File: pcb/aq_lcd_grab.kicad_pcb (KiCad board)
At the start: 4 copper layers, 32 x 50 mm, 29 parts, among them J1 Conn_01x39_Socket, J2 Conn_01x39_Socket, J3 Conn_01x03_Socket, J4 Conn_01x02_Socket, J5 Conn_01x03_Pin, U1 STM32F103C8Tx, U2 Conn_01x14

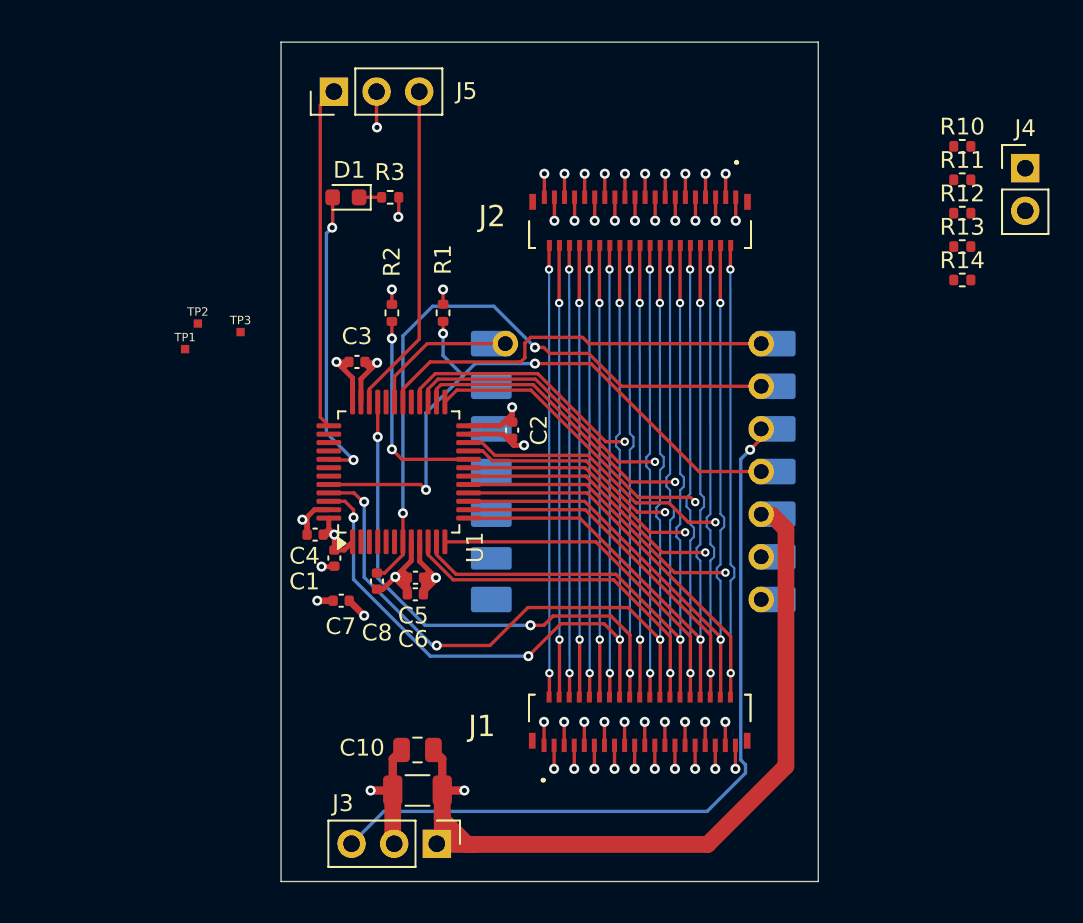
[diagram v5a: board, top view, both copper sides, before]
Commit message: PCB: routing pass — more traces, placement nudges, zone refill
Manual layout work on the KiCad PCB: ~32 net-new trace segments,
a couple of additional vias, and ~80 placement adjustments. Zone
fills recomputed against the new geometry. No SKiDL/netlist
changes — this is layout work on top of the existing netlist.

Co-Authored-By: Claude Opus 4.7 (1M context) <noreply@anthropic.com>
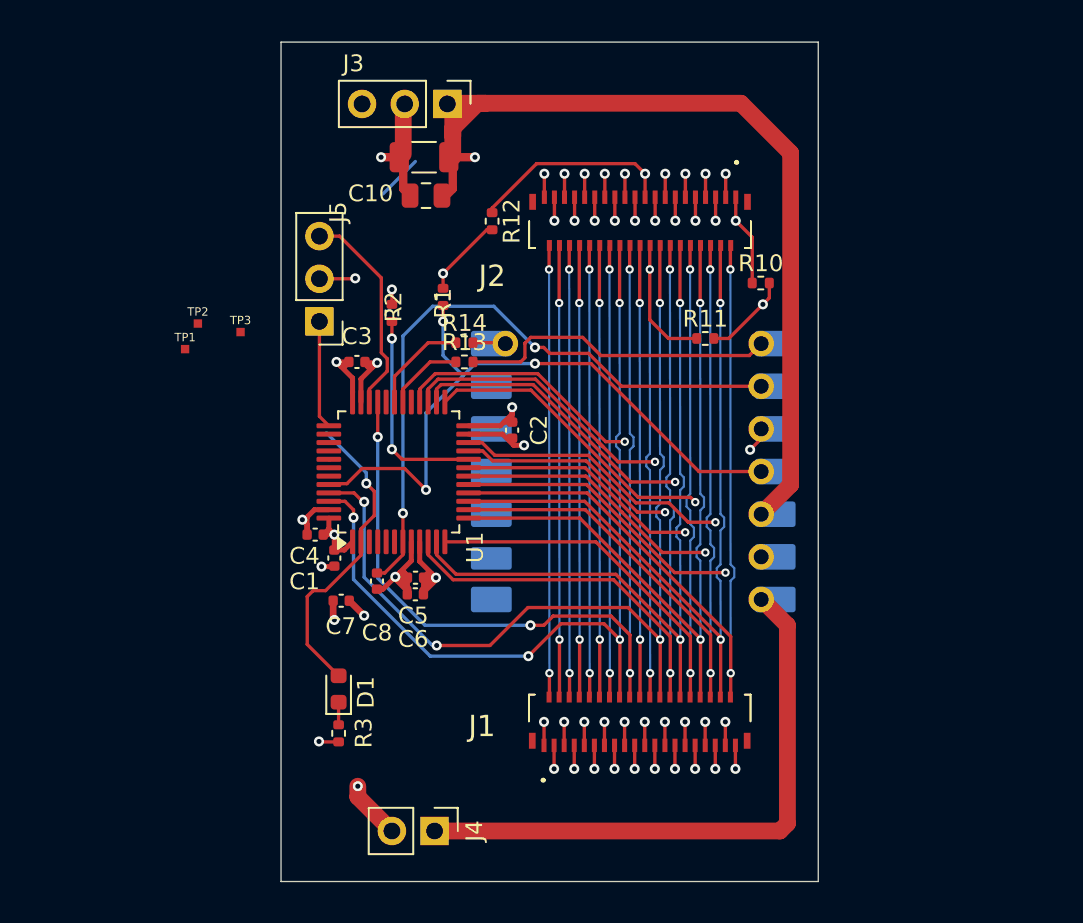
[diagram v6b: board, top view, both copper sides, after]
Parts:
- moved J4 52.9 mm to (59.9, 72.4), turned to -90 degrees
- moved J3 44.1 mm to (60.7, 29.1)
- moved C11 37.7 mm to (59.3, 32.3)
- moved C10 33.0 mm to (59.4, 34.5)
- moved R3 32.1 mm to (54.2, 66.6), turned to 90 degrees
- moved R13 30.4 mm to (61.7, 44.5)
- moved R14 29.9 mm to (61.7, 43.3)
- moved D1 29.3 mm to (54.2, 63.9), turned to 90 degrees
- moved R12 28.0 mm to (63.4, 36.1), turned to -90 degrees
- moved R11 18.0 mm to (76.1, 43.1)
- moved R10 14.5 mm to (79.4, 39.8)
- moved J5 13.7 mm to (53.1, 42.0), turned to 180 degrees
- moved R1 0.95 mm to (60.5, 40.6)
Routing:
- net PIC32_RESET: track 46.3 -> 4.24 mm
- net +5V: track 0.00 -> 35.2 mm
- net UART_STM_TX: track 24.0 -> 4.59 mm
- net UART_ESP_RX: track 0.00 -> 19.0 mm
- net SWCLK: track 20.5 -> 6.45 mm
- net GND: track 31.1 -> 43.8 mm, vias 10 -> 12
- net GND_19: track 36.1 -> 46.9 mm
- net SWDIO: track 19.7 -> 12.7 mm
- net GND_18: track 27.0 -> 33.3 mm
- net +3V3: track 70.1 -> 76.2 mm
- net GND_1: track 35.8 -> 39.9 mm
- net UART_STM_RX: track 8.94 -> 6.01 mm
- net UART_ESP_TX: track 0.00 -> 1.95 mm
- net BOOT0: track 38.1 -> 39.8 mm
- net LED_STATUS: track 18.0 -> 18.5 mm, vias 2 -> 1

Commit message: treewide: use TIM2/PA0 for WR on both bench rig and PCB; align pin mapping
TIM1_ETR can only remap to PE7 (not present on LQFP-48), so PA12 was
never a viable PCB option.  Commit to TIM2/PA0 for both boards so one
firmware covers both.

Update CAPTURE_TAP in aq_lcd_grab.py to mirror the bench-rig routing
exactly (PB5–PB12=DB0–DB7, PB0/PB1=DB14/DB15, PB13/PB14=DB9/DB10,
PB15=DC, PA1=DB8, PA2–PA4=DB11–DB13, PA5=CS), regenerate netlist.
Replace test point TP3 from PB5 (now DB0) to PA6.

Update docs/pcb_spec.md: TIM2 capture mechanism, DMA channel table,
suggested-allocation table reordered by flex pin number, pin pools and
free-pool list corrected.

Update firmware-stm32/README.md and capture.rs: remove the "PCB will
switch to TIM1/PA12" caveat.

Co-Authored-By: Claude Sonnet 4.6 <noreply@anthropic.com>
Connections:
- TP3 pad 1: PB5 -> PA6
- U1 pad 10: DB12 -> WR
- U1 pad 11: DB10 -> DB8
- U1 pad 12: DB8 -> DB11
- U1 pad 13: DB6 -> DB12
- U1 pad 14: DB4 -> DB13
- U1 pad 15: DB2 -> CS
- U1 pad 16: DB0 -> PA6
- U1 pad 17: DB1 -> (no net)
- U1 pad 18: DB5 -> DB14
- U1 pad 19: DB9 -> DB15
- U1 pad 21: DB13 -> DB5
- U1 pad 22: DB3 -> DB6
- U1 pad 26: DB11 -> DB9
- U1 pad 27: DB15 -> DB10
- U1 pad 33: WR -> (no net)
- U1 pad 41: PB5 -> DB0
- U1 pad 42: (no net) -> DB1
- U1 pad 43: (no net) -> DB2
- U1 pad 45: DB14 -> DB3
- U1 pad 46: CS -> DB4

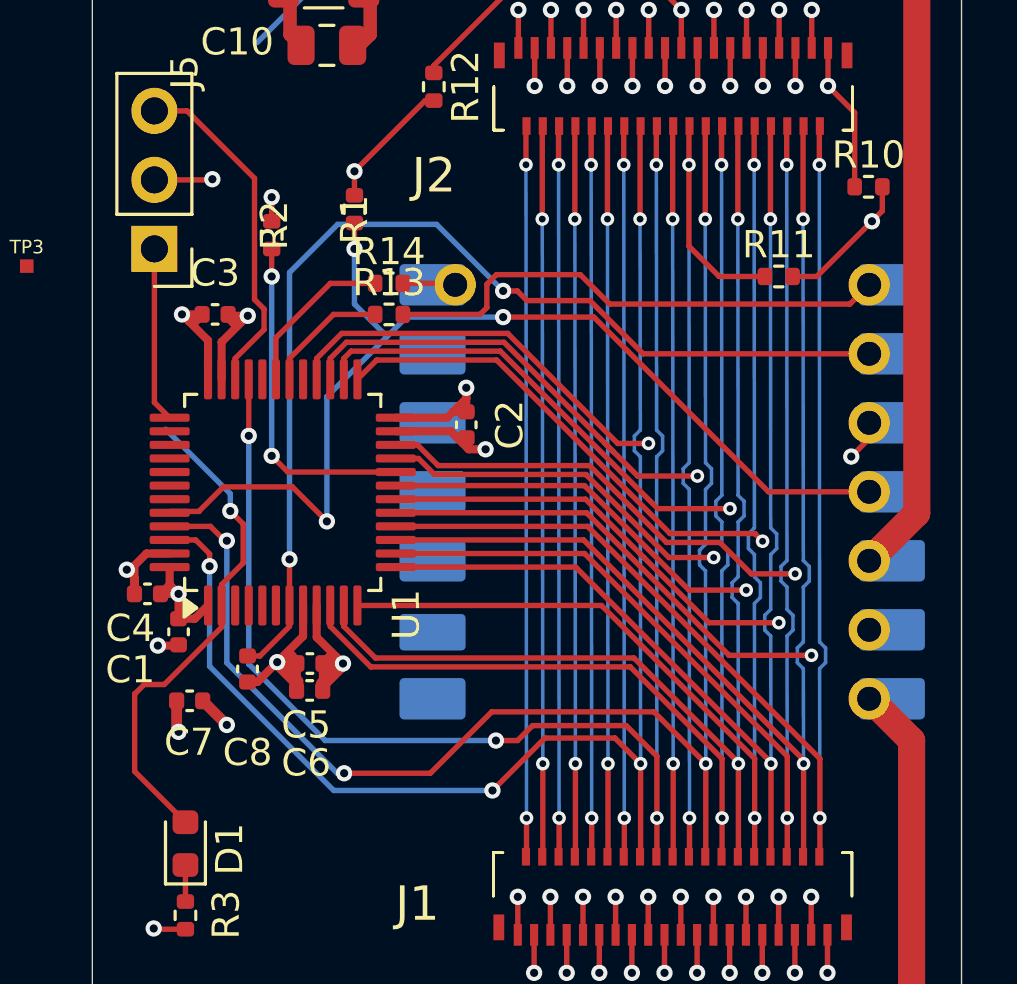
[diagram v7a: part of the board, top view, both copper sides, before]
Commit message: pcb/route_lcd_bus: add escape vias for first-row nets; kink In2.Cu around them
- EXTRA_ESCAPE_VIAS replaces the single DC entry with a hardcoded list of
  (net, y) pairs, making it easy to adjust positions. DC, DB10, DB9, DB7,
  DB6, DB5, DB15, DB14 now each get an escape via placed at an explicit y.
- DB7 and DB9 removed from ODD_DB_ESCAPE_ORDER; their escape vias are now
  managed via EXTRA_ESCAPE_VIAS along with DC and the even-DB nets.
- ESCAPE_Y_START bumped to 57.6 so the topmost odd-DB via stays below the
  new first-row cluster.
- dodge_mid_obstacles(): new helper that injects 45° doglegs into an
  existing polyline for obstacles in the middle stretch. Called from
  route_with_plan() so In2.Cu traces kink around escape vias that fall
  between the two fanout regions.
- Escape via waypoints spliced into the In2.Cu polyline so KiCad shows
  an explicit connection point at each escape via.
- Fix EXTRA_ESCAPE_VIAS flex-pair detection to use FLEX_BAND_YS (all
  bands) instead of only deep-band y values, so even-DB nets like DB10
  are found correctly.
- Deduplicate the deletes list before applying events to prevent double
  deletion when a net appears in both ODD_DB_ESCAPE_ORDER and
  EXTRA_ESCAPE_VIAS, which caused PCB file corruption.

Co-Authored-By: Claude Sonnet 4.6 <noreply@anthropic.com>
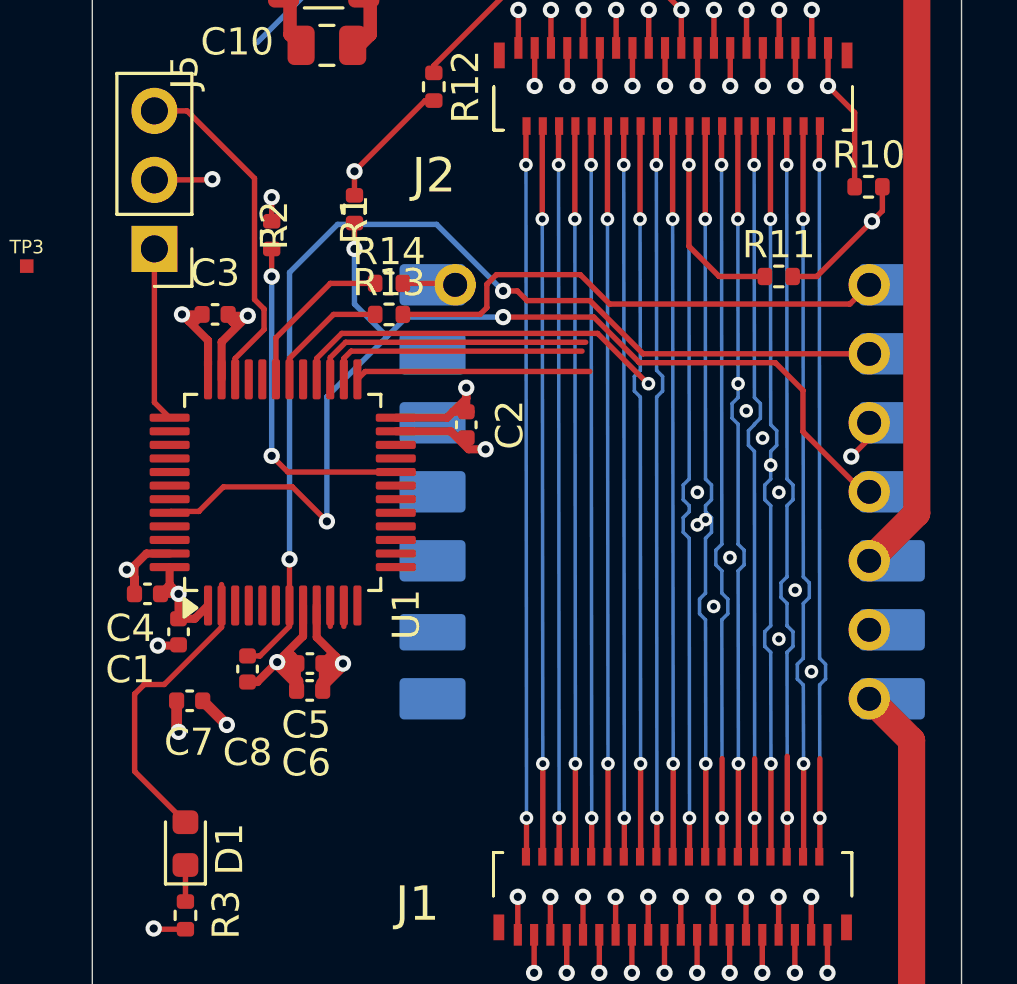
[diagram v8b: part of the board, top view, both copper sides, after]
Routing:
- net WR: track 56.7 -> 27.8 mm, vias 4 -> 2
- net DB14: track 54.7 -> 27.0 mm, vias 4 -> 3
- net CS: track 51.4 -> 26.6 mm, vias 4 -> 2
- net DB0: track 48.4 -> 29.3 mm
- net DB2: track 45.3 -> 27.0 mm
- net DB1: track 53.6 -> 36.1 mm
- net DB11: track 53.6 -> 36.3 mm
- net DB4: track 47.0 -> 29.7 mm
- net DB12: track 46.6 -> 29.4 mm
- net DB15: track 53.1 -> 36.3 mm, vias 3 -> 4
- net DB3: track 52.8 -> 36.1 mm
- net DB6: track 43.7 -> 27.0 mm, vias 2 -> 3
- net DB8: track 46.4 -> 30.2 mm
- net DB5: track 52.1 -> 36.3 mm, vias 3 -> 4
- net DB13: track 49.3 -> 36.3 mm
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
